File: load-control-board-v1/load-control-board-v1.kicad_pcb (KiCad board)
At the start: 2 copper layers, 100 x 100 mm, 173 parts, among them Q1 AO3400A, Q10 AO3400A, Q11 AO3400A, Q12 IRFP7530PBF, Q2 AO3400A, Q3 IRFP7530PBF, Q4 AO3400A, Q5 AO3400A, Q6 IRFP7530PBF, Q7 AO3400A, Q8 AO3400A, Q9 IRFP7530PBF, U1 LM317_SOT-223, U10 OPA188xxDBV, U11 OPA188xxDBV, U12 INA186A1IDCKR, U13 OPA188xxDBV, U14 OPA188xxDBV, U15 INA186A1IDCKR, U16 OPA188xxDBV, U17 OPA188xxDBV, U18 INA186A1IDCKR, U19 OPA188xxDBV, U2 74AHC1G04, U20 OPA188xxDBV, U21 INA186A1IDCKR, U22 TL081HIDR, U3 LM317_SOT-223, U5 REF5025AD, U6 SN74LVC1G123DCUR_C352969, U7 TL081HIDR, U8 OPA188xxDBV, U9 PZ127-2-10-S

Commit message: initial layout
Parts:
- removed C22, C24, C31, C33, C40, C42: 100p, Capacitor_SMD:C_0603_1608Metric
- removed C23, C26, C30, C32, C35, C39, C41, C44, C48: 100n, Capacitor_SMD:C_0603_1608Metric
- removed C25, C34, C43: 47n, Capacitor_SMD:C_0603_1608Metric
- removed C27, C36, C45: 1n, Capacitor_SMD:C_0603_1608Metric
- removed C28, C29, C37, C38, C46, C47: 10n, Capacitor_SMD:C_0603_1608Metric
- removed Q10, Q11, Q4, Q5, Q7, Q8: AO3400A, programmable-load-library:SOT-23-3_L2.9-W1.3-P1.90-LS2.4-BR
- removed Q12, Q6, Q9: IRFP7530PBF, programmable-load-library:PG-TO247-3_L15.9-W5.2-P5.44-L
- removed R30, R34, R44, R48, R58, R62: 50k, Resistor_SMD:R_0603_1608Metric
- removed R31, R32, R36, R39, R45, R46, R50, R53, R59, R60, R64, R67: 1k, Resistor_SMD:R_0603_1608Metric
- removed R33, R38, R41, R42, R47, R52, R55, R56, R61, R66, R69, R70: 0, Resistor_SMD:R_0603_1608Metric
- removed R35, R49, R63: 47, Resistor_SMD:R_0603_1608Metric
- removed R37, R51, R65: 500, Resistor_SMD:R_0603_1608Metric
- removed R40, R54, R68: 100, Resistor_SMD:R_0603_1608Metric
- removed R43, R57, R71: 10k, Resistor_SMD:R_0603_1608Metric
- removed R_SHUNT2, R_SHUNT3, R_SHUNT4: BVB-M-R001-1.0, programmable-load-library:RES-SMD_4P-L6.9-W6.6_SBB-K-2F-N-T5
- removed TP0a2, TP0a3, TP0a4, TP0c2, TP0c3, TP0c4, TP4, TP5, TP6, TP7, TP8, TP9: TestPoint, TestPoint:TestPoint_Keystone_5015_Micro_Mini
- removed U13, U14, U16, U17, U19, U20: OPA188xxDBV, Package_TO_SOT_SMD:TSOT-23-5
- removed U15, U18, U21: INA186A1IDCKR, programmable-load-library:SC-70-6_L2.2-W1.3-P0.65-LS2.1-BR
- moved C49 101.2 mm to (95.8, 121.2), turned to 90 degrees
- moved R11 99.1 mm to (84.3, 121.2), turned to 90 degrees
- moved C8 98.2 mm to (74.3, 121.2), turned to -90 degrees
- moved R12 97.5 mm to (85.8, 121.2), turned to -90 degrees
- moved C4 88.9 mm to (81.5, 111.2), turned to 90 degrees
- moved C1 88.9 mm to (81.3, 103.7), turned to 90 degrees
- moved C6 88.9 mm to (89.0, 109.8), turned to 90 degrees
- moved C3 88.8 mm to (89.0, 102.2), turned to 90 degrees
- moved U5 84.0 mm to (79.3, 120.4)
- moved U22 83.8 mm to (91.0, 121.4), turned to -90 degrees
- moved R6 83.4 mm to (85.8, 107.0), turned to 180 degrees
- moved R3 81.3 mm to (82.2, 99.5), turned to 180 degrees
- moved U3 80.6 mm to (85.5, 110.5)
- moved U1 79.4 mm to (85.5, 103.0)
- moved R7 79.3 mm to (82.3, 107.0), turned to 180 degrees
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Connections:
- C3 pad 1: READY -> +5V
- R2 pad 1: READY -> +5V
- U1 pad 2: READY -> +5V
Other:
- board text removed: "INA"
- board text removed: "differential"
- board text removed: "logic"
- board text removed: "negative feedback"
- board text removed: "signal go though low side"

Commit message: final layout and initial connecting
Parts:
- moved TP3 70.6 mm to (125.6, 75.1)
- moved TP0c1 52.0 mm to (106.5, 86.1)
- moved TP0a1 48.0 mm to (108.8, 103.0)
- moved TP2 47.9 mm to (108.9, 97.9)
- moved TP1 15.2 mm to (72.9, 104.4)
- moved R_SHUNT1 6.84 mm to (137.0, 103.3)
- moved C19 3.05 mm to (118.0, 84.7)
- moved C13 1.15 mm to (117.1, 102.5)
- moved R16 1.03 mm to (117.6, 104.1)
- moved R19 0.98 mm to (118.0, 81.9)
- moved Q1 0.51 mm to (114.7, 81.1)
- moved R25 0.30 mm to (115.8, 87.9), turned to 90 degrees
- moved C15 0.19 mm to (120.5, 98.0)
- moved R20 0.14 mm to (120.5, 99.6)
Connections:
- R21 pad 1: Net-(C15-Pad1) -> Net-(R21-Pad1)
- R21 pad 2: Net-(R21-Pad2) -> Net-(C15-Pad1)
- R22 pad 2: Net-(C15-Pad1) -> Net-(R21-Pad1)
- R23 pad 2: Net-(C15-Pad1) -> Net-(R21-Pad1)
- TP2 pad 1: Net-(R21-Pad2) -> Net-(C15-Pad1)
- U10 pad 1: Net-(R21-Pad2) -> Net-(C15-Pad1)
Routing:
- net +9V: track 0.00 -> 107.8 mm, vias 0 -> 6
- net +5V: track 0.00 -> 104.1 mm, vias 0 -> 8
- net READY: track 0.00 -> 88.7 mm, vias 0 -> 2
- net GND: track 0.00 -> 74.1 mm, vias 0 -> 54
- net VBUS: track 0.00 -> 60.6 mm
- net ~{ENABLE}: track 0.00 -> 41.8 mm, vias 0 -> 2
- net V_REF: track 0.00 -> 39.7 mm
- net /ch0/MOS_G: track 0.00 -> 29.6 mm
- net /ch0/V_Rs0p: track 0.00 -> 23.1 mm, vias 0 -> 2
- net /ch0/V_Rs0n: track 0.00 -> 20.5 mm, vias 0 -> 2
- net Net-(C15-Pad1): track 0.00 -> 17.6 mm
- net I_CONTROL: track 0.00 -> 15.9 mm, vias 0 -> 2
- net +12V: track 0.00 -> 12.7 mm
- net Net-(U11--): track 0.00 -> 12.1 mm
- net /I_SINK_MON_CH0: track 0.00 -> 11.7 mm
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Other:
- copper layers 2 -> 4

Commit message: Import from Dong's windows computer lib
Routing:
- net GND: track 74.1 -> 71.9 mm, vias 54 -> 52
- added copper zone on In2.Cu, net GND
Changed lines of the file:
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@@
 	)
 	(segment
-		(start 59.0804 94.463)
-		(end 58.6216 94.9218)
-		(width 0.3)
-		(layer "F.Cu")
-		(net 1)
-	)
-	(segment
 		(start 86.2568 122.5788)
 		(end 85.852 122.174)
@@
 	)
 	(segment
-		(start 58.2168 94.517)
-		(end 58.6216 94.9218)
-		(width 0.3)
-		(layer "F.Cu")
-		(net 1)
-	)
-	(segment
 		(start 89.4588 100.9912)
 		(end 89 101.45)
@@
 	)
 	(segment
-		(start 59.0804 94.005)
-		(end 59.0804 94.463)
-		(width 0.3)
-		(layer "F.Cu")
-		(net 1)
-	)
-	(segment
 		(start 80.8752 102.4144)
 		(end 81.28 102.8192)
@@
 	)
 	(segment
-		(start 58.2168 94.005)
-		(end 58.2168 94.517)
-		(width 0.3)
-		(layer "F.Cu")
-		(net 1)
-	)
-	(segment
 		(start 79.1938 70.2752)
 		(end 79.5848 70.2752)
@@
 	)
 	(via
-		(at 58.2168 94.005)
-		(size 0.8)
-		(drill 0.4)
-		(layers "F.Cu" "B.Cu")
-		(net 1)
-	)
-	(via
 		(at 80.3632 99.0584)
 		(size 0.8)
@@
 	)
 	(via
-		(at 59.0804 94.005)
-		(size 0.8)
-		(drill 0.4)
-		(layers "F.Cu" "B.Cu")
-		(net 1)
-	)
-	(via
 		(at 114.1476 82.9064)
 		(size 0.8)
@@
 		(net 70)
 	)
+	(zone
+		(net 1)
+		(net_name "GND")
+		(layer "In2.Cu")
+		(hatch edge 0.5)
+		(connect_pads yes
+			(clearance 0.5)
+		)
+		(min_thickness 0.25)
+		(filled_areas_thickness no)
+		(fill yes
+			(thermal_gap 0.5)
+			(thermal_bridge_width 0.5)
+			(smoothing fillet)
+			(radius 0.5)
+		)
+		(polygon
+			(pts
+				(xy 157.0228 40.386) (xy 158.8516 42.2148) (xy 158.8516 141.4272) (xy 154.6352 145.6436) (xy 54.102 145.6436)
+				(xy 50.3428 141.8844) (xy 50.3428 42.0116) (xy 51.9684 40.386)
+			)
+		)
+	)
 	(embedded_fonts no)

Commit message: Add connector
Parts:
- added TP10: +5v, TestPoint:TestPoint_Keystone_5015_Micro_Mini, F.Cu at (94.0, 103.0)
- added TP11: +12v, TestPoint:TestPoint_Keystone_5015_Micro_Mini, F.Cu at (94.0, 110.2)

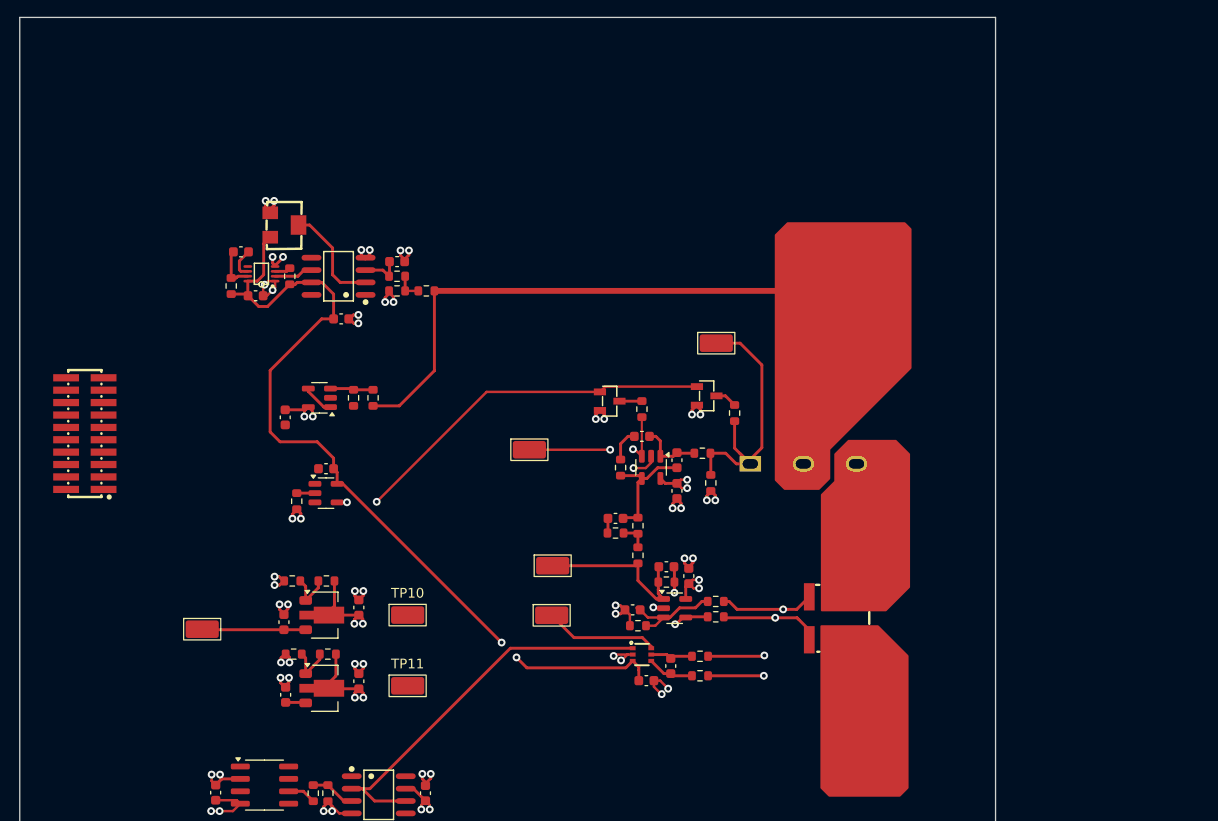
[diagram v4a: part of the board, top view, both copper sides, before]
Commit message: Define the connector pinout to control board, import current connector
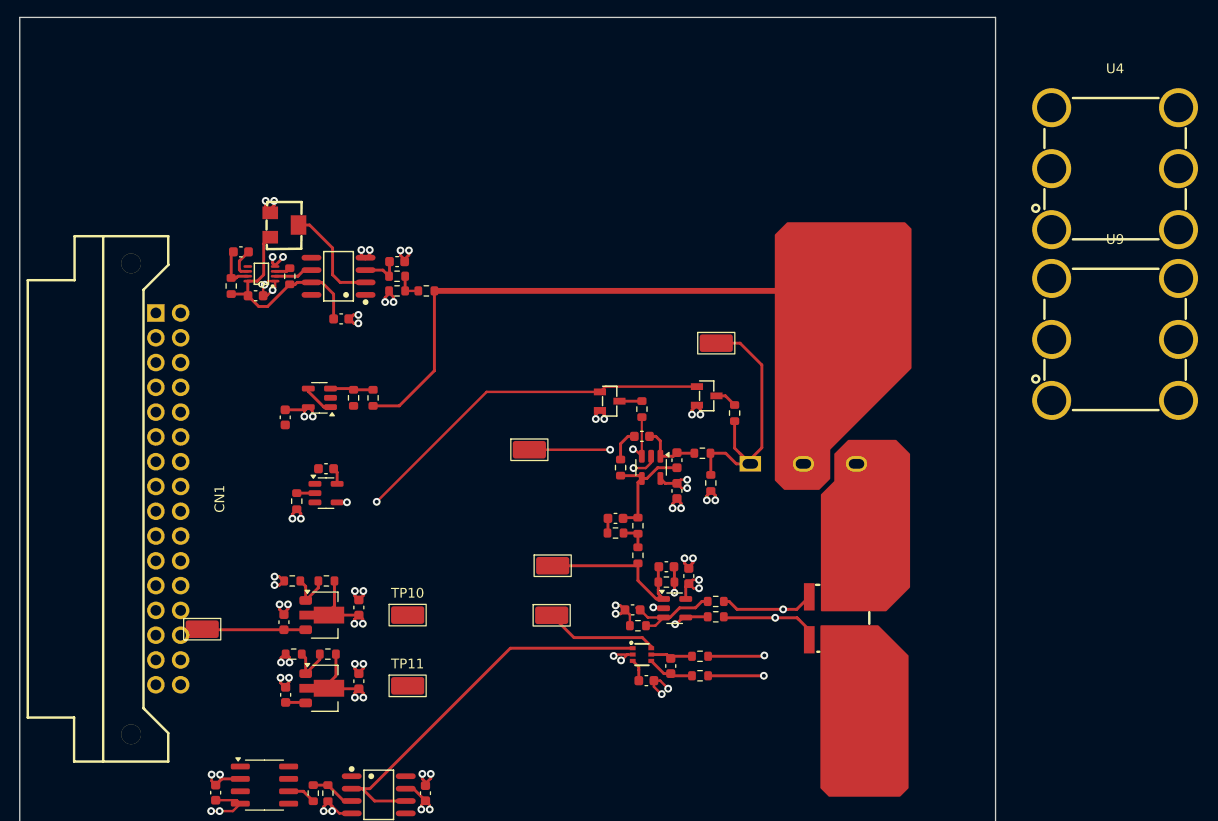
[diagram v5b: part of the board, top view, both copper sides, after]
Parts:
- added CN1: 3511232BMRS0BNA2, programmable-load-library:CONN-TH_3511232BMRS0BNA2, F.Cu at (69.5, 91.1)
- added U4: TT56145145-1520, programmable-load-library:TH_6P-TT56145145-1500, F.Cu at (166.5, 57.2)
- TP11: value +12v -> +9v
- U9: value PZ127-2-10-S -> TT56145145-1520; footprint programmable-load-library:HDR-SMD_PZ127-2-10-S -> programmable-load-library:TH_6P-TT56145145-1500
- moved U9 106.0 mm to (166.5, 74.8), turned to 0 degrees
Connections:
- net READY renamed 5V
- U12 pad 1: V_REF -> /ch0/V_REF_FIL
- U6 pad 5: unconnected-(U6-Q-Pad5) -> OV_ALERT
- U9 pad 1: unconnected-(U9-Pad1) -> GND
- U9 pad 2: unconnected-(U9-Pad2) -> GND
- U9 pad 3: unconnected-(U9-Pad3) -> GND
- U9 pad 4: unconnected-(U9-Pad4) -> GND
- U9 pad 5: unconnected-(U9-Pad5) -> GND
- U9 pad 6: unconnected-(U9-Pad6) -> GND
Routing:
- net 5V: track 88.7 -> 26.7 mm, vias 2 -> 0
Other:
- board text added: "LDO might need some heat dissapate consideration"
- board text added: "Move this closer to VBUS power trace Change sample point to the terminal(where the copper wire connect) of VBUS"
- board text added: "Move voltage reference closer to INA186 Make a guard trace GND for V_REF Place the LPF near INA186"
- board text added: "Need to change the board edge to match the connector!"

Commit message: layout before check
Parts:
- added C11: 100n, Capacitor_SMD:C_0603_1608Metric, F.Cu at (111.0, 107.7)
- added C53: 1u, Resistor_SMD:R_0603_1608Metric, F.Cu at (112.7, 107.7)
- added R72: 100, Resistor_SMD:R_0603_1608Metric, F.Cu at (108.3, 106.9)
- moved U9 49.5 mm to (141.5, 117.4)
- moved U4 28.8 mm to (139.3, 66.9)
- moved U22 15.0 mm to (99.8, 109.3)
- moved C49 15.0 mm to (104.6, 109.1)
- moved C8 15.0 mm to (83.1, 109.0)
- moved R11 15.0 mm to (93.1, 109.1)
- moved R12 15.0 mm to (94.6, 109.1)
- moved U5 15.0 mm to (88.1, 108.3)
- moved C4 8.59 mm to (75.0, 116.8)
- moved C6 8.59 mm to (82.5, 115.4)
- moved R6 8.59 mm to (79.3, 112.6)
- moved R7 8.59 mm to (75.8, 112.6)
- moved TP11 8.59 mm to (87.5, 115.9)
- moved U3 8.59 mm to (79.0, 116.1)
- moved TP1 6.00 mm to (76.1, 99.4)
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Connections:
- C10 pad 2: 5V -> +5V
- C2 pad 2: 5V -> +5V
- C21 pad 2: 5V -> +5V
- C7 pad 2: 5V -> +5V
- CN1 pad 10: 5V -> +5V
- R13 pad 2: 5V -> +5V
- U12 pad 3: 5V -> +5V
- U2 pad 5: 5V -> +5V
- U6 pad 8: 5V -> +5V
- U7 pad 7: 5V -> +5V
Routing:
- net +12V: track 12.7 -> 74.5 mm, vias 0 -> 4
- net VBUS: track 60.6 -> 122.3 mm
- net +5V: track 104.1 -> 158.9 mm, vias 8 -> 17
- net OV_ALERT: track 0.00 -> 46.3 mm
- net /I_SINK_MON_CH0: track 11.7 -> 55.2 mm
- net +9V: track 107.8 -> 145.3 mm
- net I_CONTROL: track 15.9 -> 53.3 mm, vias 2 -> 4
- net V_BUS_MON: track 3.24 -> 26.9 mm, vias 0 -> 2
- net V_REF: track 39.7 -> 17.9 mm
- net ENABLE: track 1.86 -> 19.7 mm
- net GND: track 71.9 -> 82.5 mm, vias 52 -> 57
- net /ch0/V_REF_FIL: track 0.00 -> 8.38 mm
- net 5V: track 26.7 -> 22.6 mm
- net Net-(U6-Cext): track 3.16 -> 2.23 mm
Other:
- board size 100 x 100 mm -> 96.9 x 74.5 mm
- board text removed: "LDO might need some heat dissapate consideration"
- board text removed: "Move this closer to VBUS power trace Change sample point to the terminal(where the copper wire connect) of VBUS"
- board text removed: "Move voltage reference closer to INA186 Make a guard trace GND for V_REF Place the LPF near INA186"
- board text removed: "Need to change the board edge to match the connector!"

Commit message: layout adjust
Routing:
- net GND: track 82.5 -> 96.0 mm, vias 57 -> 61
- net +5V: track 158.9 -> 164.5 mm
- net ~{ENABLE}: track 41.8 -> 41.9 mm, vias 2 -> 0
- added copper zone on F.Cu, net GND
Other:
- board size 96.9 x 74.5 mm -> 99.6 x 75.3 mm

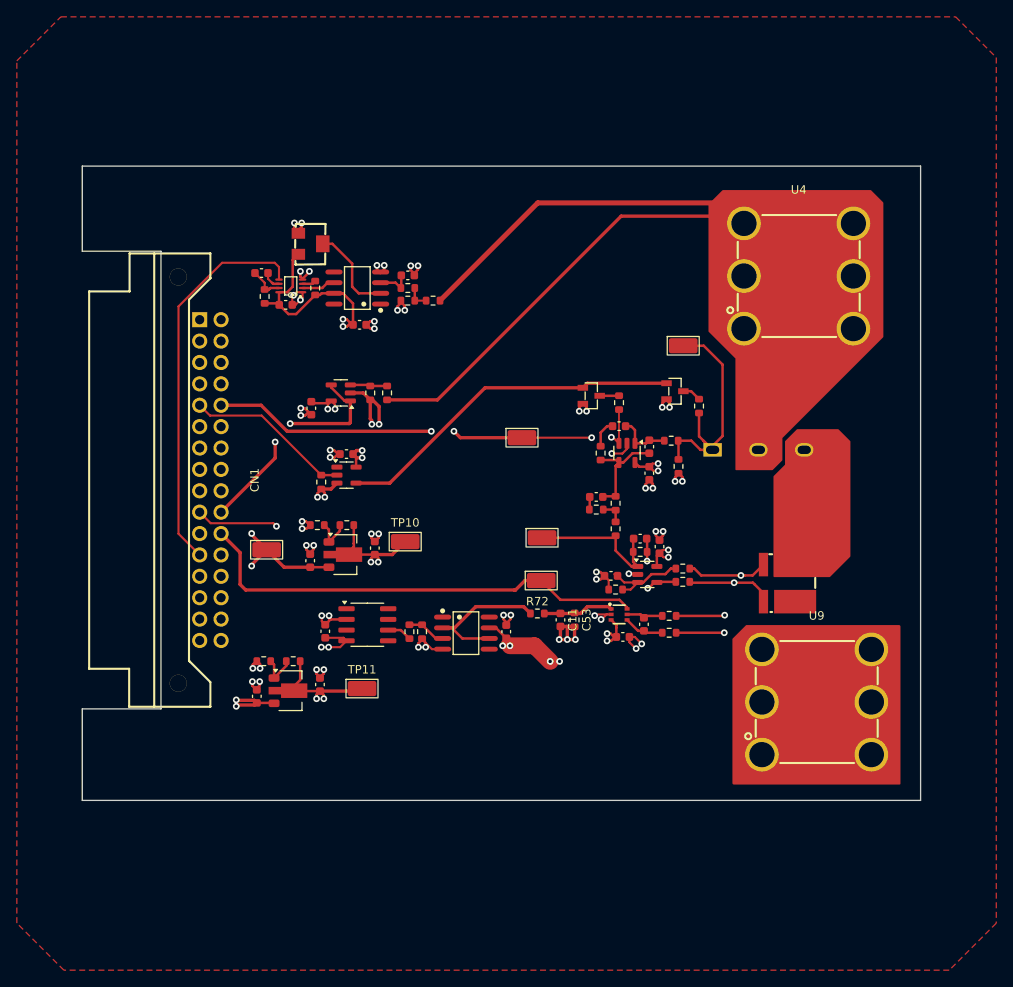
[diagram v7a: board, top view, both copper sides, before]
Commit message: Section upload
Monostable Multivibrator for OV, VBUS scale resistor network and buffer Opa
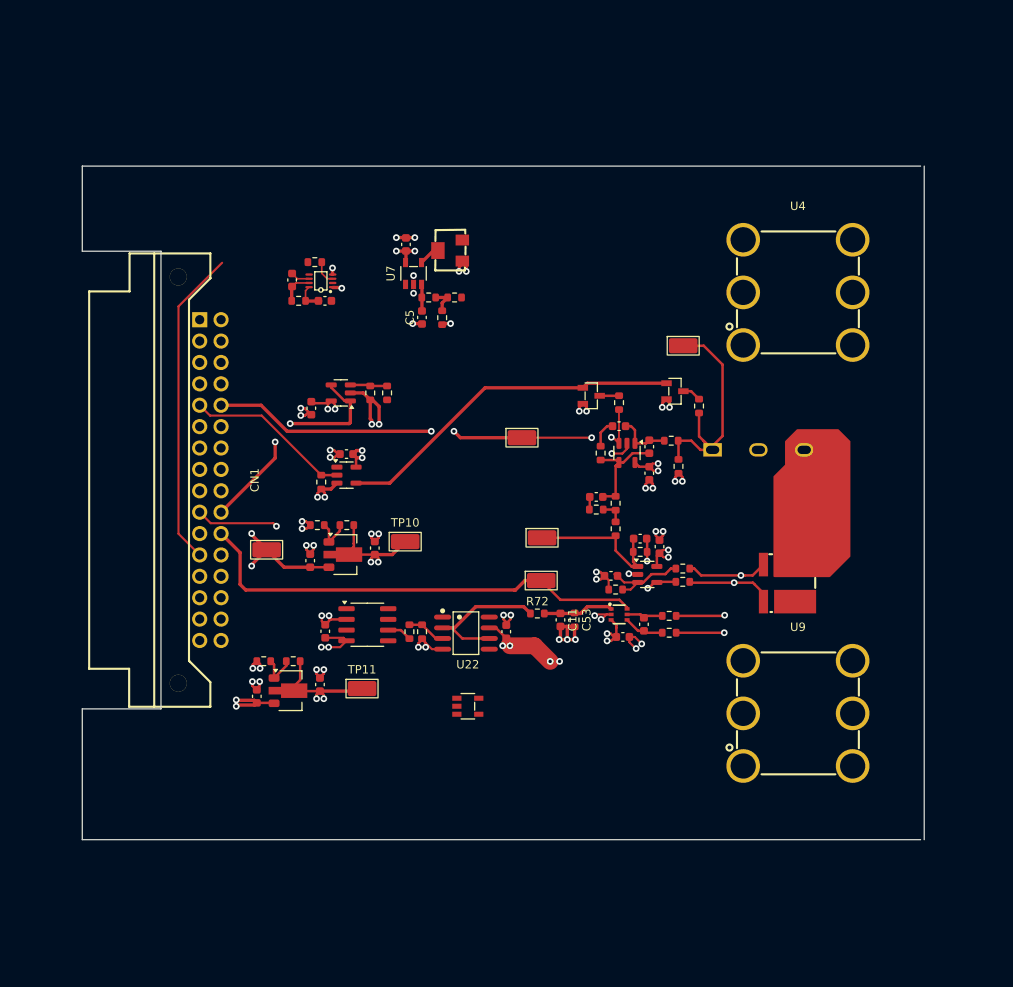
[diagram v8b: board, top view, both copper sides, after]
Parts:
- added U22: TL081HIDBVR, programmable-load-library:SOT-23-5_L2.9-W1.6-P0.95-LS2.8-TL, F.Cu at (100.0, 118.0)
- U7: value TL081HIDR -> TL081HIDBVR; footprint programmable-load-library:SOIC-8_L4.9-W3.9-P1.27-LS6.0-BL -> programmable-load-library:SOT-23-5_L2.9-W1.6-P0.95-LS2.8-TL
- moved R9 16.6 mm to (97.9, 63.8), turned to 90 degrees
- moved C7 11.0 mm to (92.7, 63.1), turned to -90 degrees
- moved U7 6.90 mm to (93.6, 66.5)
- moved C5 5.27 mm to (94.6, 71.8), turned to 90 degrees
- moved C10 4.68 mm to (83.1, 69.8)
- moved R5 4.56 mm to (97.0, 71.8), turned to 90 degrees
- moved R13 4.07 mm to (80.0, 69.8), turned to 0 degrees
- moved C9 3.73 mm to (79.2, 67.3), turned to 90 degrees
- moved U6 3.63 mm to (82.6, 67.4)
- moved R10 3.08 mm to (81.9, 65.2), turned to 0 degrees
- moved R8 2.72 mm to (95.4, 69.4)
- moved U9 2.60 mm to (139.3, 118.8)
- moved R4 2.58 mm to (98.5, 69.4)
- moved U4 1.95 mm to (139.3, 68.8)
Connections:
- U7 pad 1: unconnected-(U7-NC-Pad1) -> Net-(U6-B)
- U7 pad 2: Net-(U7-IN-) -> GND
- U7 pad 4: GND -> Net-(U7-IN-)
- U7 pad 5: unconnected-(U7-NC-Pad5) -> +5V
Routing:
- net VBUS: track 122.3 -> 0.00 mm
- net +9V: track 145.3 -> 27.0 mm
- net +5V: track 164.5 -> 69.3 mm
- net +12V: track 74.5 -> 20.8 mm
- net 5V: track 22.6 -> 0.00 mm
- net GND: track 96.0 -> 86.6 mm, vias 61 -> 57
- net OV_ALERT: track 46.3 -> 37.9 mm
- net Net-(U7-IN-): track 10.9 -> 2.54 mm
- net Net-(U6-B): track 3.99 -> 0.00 mm
- net Net-(U10--): track 9.63 -> 6.40 mm
- net Net-(U6-~{CLR}): track 1.63 -> 2.69 mm
- net Net-(U7-IN+): track 4.19 -> 3.17 mm
- removed copper zone on F.Cu, net GND
- removed copper zone on In2.Cu, net GND
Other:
- board size 99.6 x 75.3 mm -> 100 x 80 mm
- board text added: "Align the connector and board edge"
- board text added: "Keep AGND and PGND single point connection"
- board text added: "Layout - Align the VBUS terminal and GND terminal"
- board text added: "Monostable Multivibrator for OV"
- board text added: "Move READY block to the top of VBUS MONITOR block"
- board text added: "Powerrail: 5V - Keep power trace as straght as possible"
- board text added: "TODO list"
- board text added: "Use the same trace width for same function net"
- board text added: "VBUS scale resistor network and buffer Opa"
